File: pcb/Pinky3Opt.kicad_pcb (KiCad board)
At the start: 2 copper layers, 276.2 x 126 mm, 160 parts, among them J1 USB_C_Receptacle_USB2.0, J2 Conn_01x04, J3 USB_C_Receptacle_USB2.0, J4 Conn_01x04, SW1 Reset, SW2 Reset, U1 ATmega32U4-A, U2 PRTR5V0U2X, U3 ATmega32U4-A, U4 PRTR5V0U2X, Y1 16MHz, Y2 16MHz

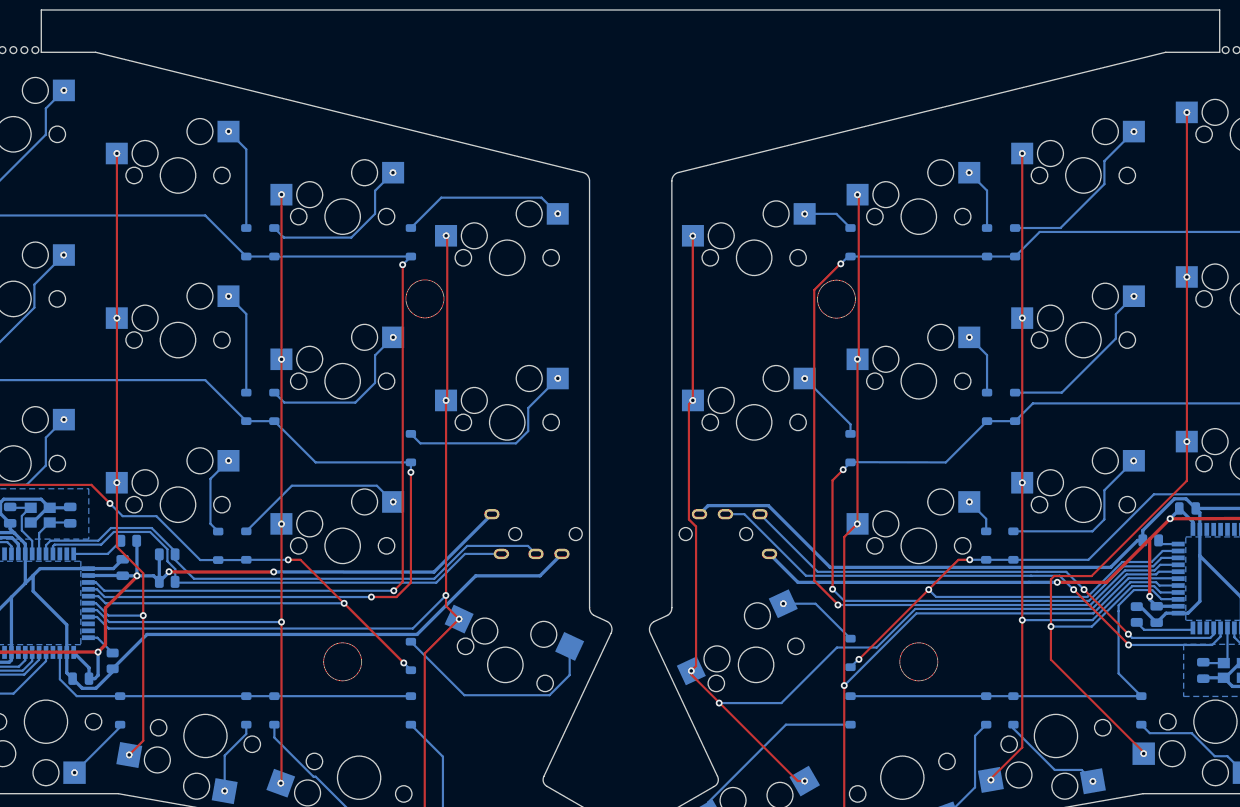
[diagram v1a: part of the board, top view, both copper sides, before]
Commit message: trrs bottom side
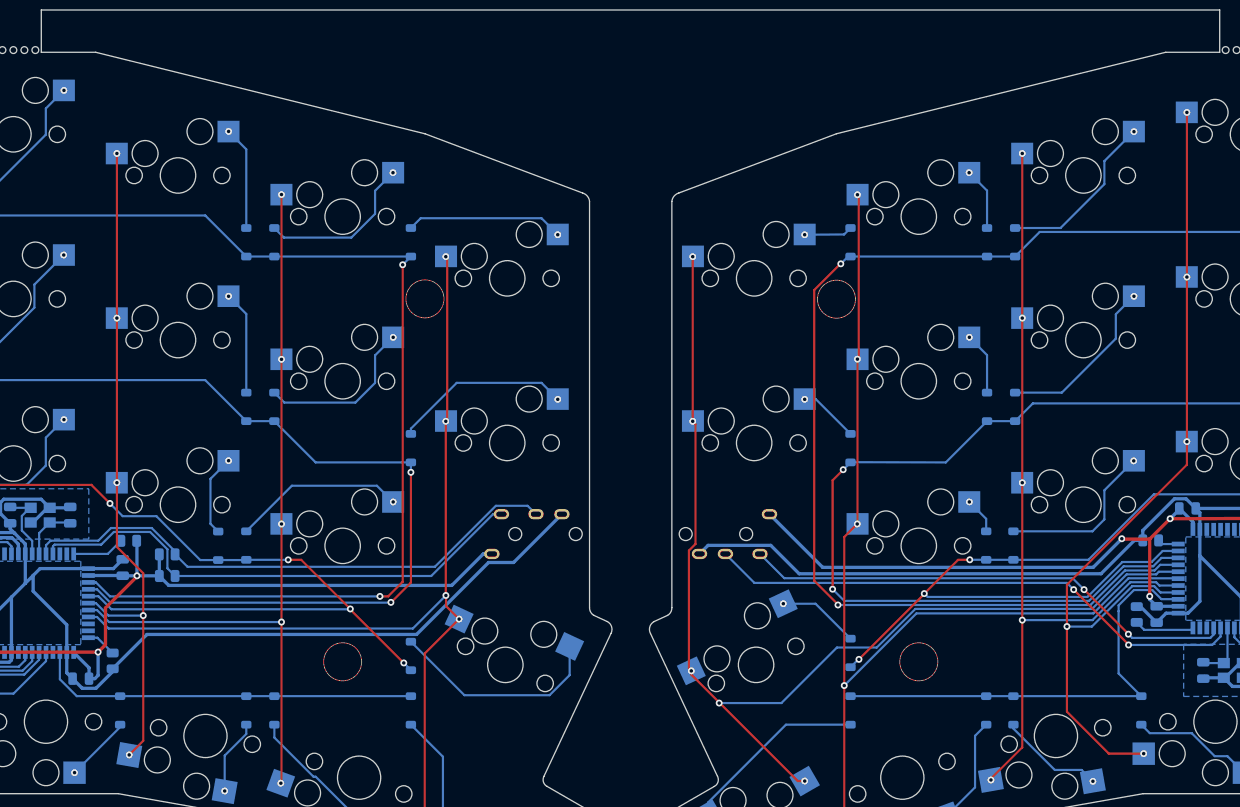
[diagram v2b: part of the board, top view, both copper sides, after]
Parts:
- J2, J4: moved to B.Cu
- moved MX14 2.38 mm to (152.4, 88.1)
- moved MX26 2.38 mm to (181.0, 69.1)
- moved MX33 2.38 mm to (181.0, 88.1)
- moved MX7 2.38 mm to (152.4, 69.1)
- moved R8 0.68 mm to (113.0, 103.5)
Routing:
- net /COL3_R: track 104.7 -> 101.1 mm
- net /COL0_R: track 129.2 -> 126.6 mm
- net /COL6_L: track 115.4 -> 113.0 mm
- net /SDA_R: track 59.4 -> 57.4 mm
- net /SCL_R: track 65.2 -> 63.3 mm
- net GND: track 254.1 -> 255.9 mm
- net +5V: track 123.4 -> 121.7 mm, vias 6 -> 4
- net Net-(D33-A): track 8.61 -> 7.01 mm
- net Net-(D14-A): track 22.2 -> 20.6 mm
- net GNDA: track 269.1 -> 267.8 mm
- net Net-(D7-A): track 19.3 -> 18.3 mm
- net /ROW2_L: track 140.9 -> 141.9 mm
- net /SDA_L: track 59.0 -> 59.8 mm
- net /ROW0_L: track 176.4 -> 176.9 mm
- net /ROW1_L: track 155.4 -> 156.0 mm
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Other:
- outline, holes or cut-outs redrawn
